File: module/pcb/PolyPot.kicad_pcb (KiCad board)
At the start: 2 copper layers, 50 x 50 mm, 43 parts, among them J1 V_BAT_1S, J2 PROG/DEBUG, J3 HUMIDITY_CONN, J4 TOF_DIST_SENS, J5 M3, J6 M3, J7 M3, J8 M3, J9 LUMINOSITY_CONN, M1 DC_WATER_PUMP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

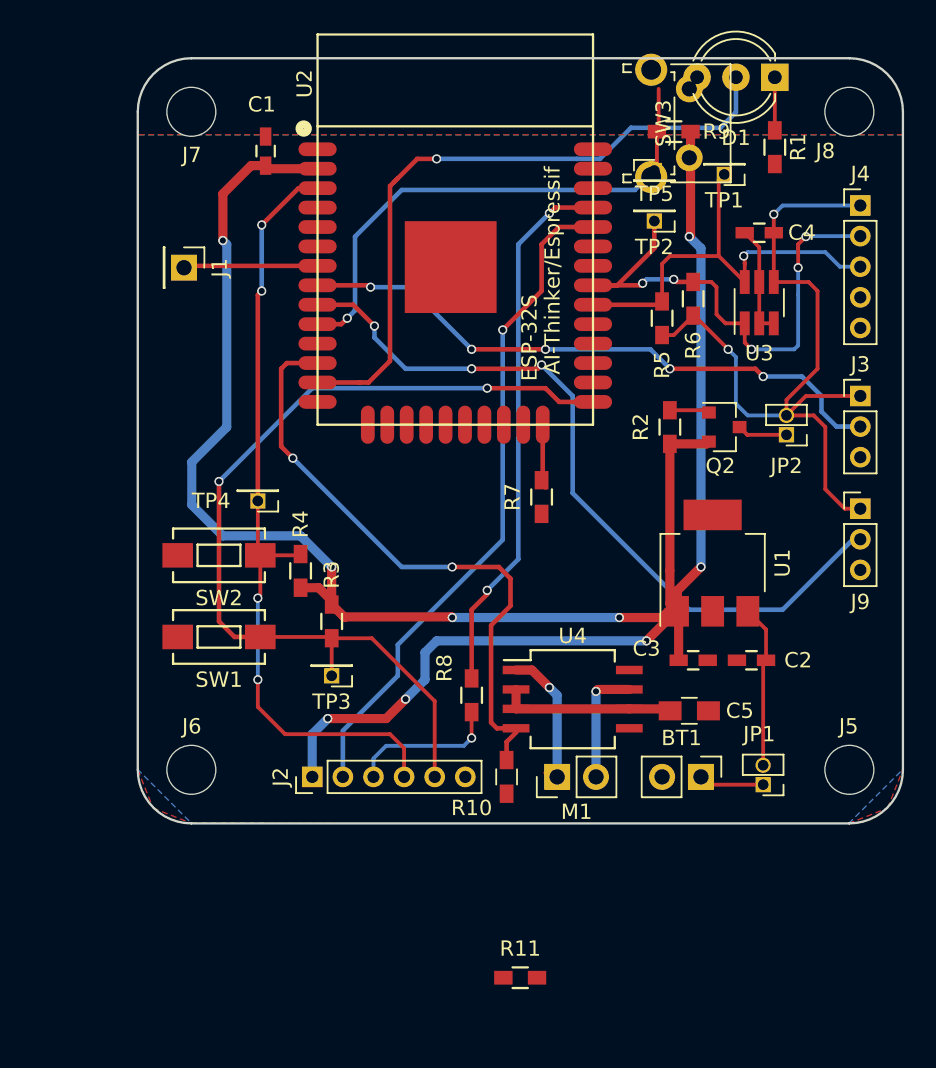
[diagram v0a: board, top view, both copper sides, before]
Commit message: PCB: change SOIC-8 footprint
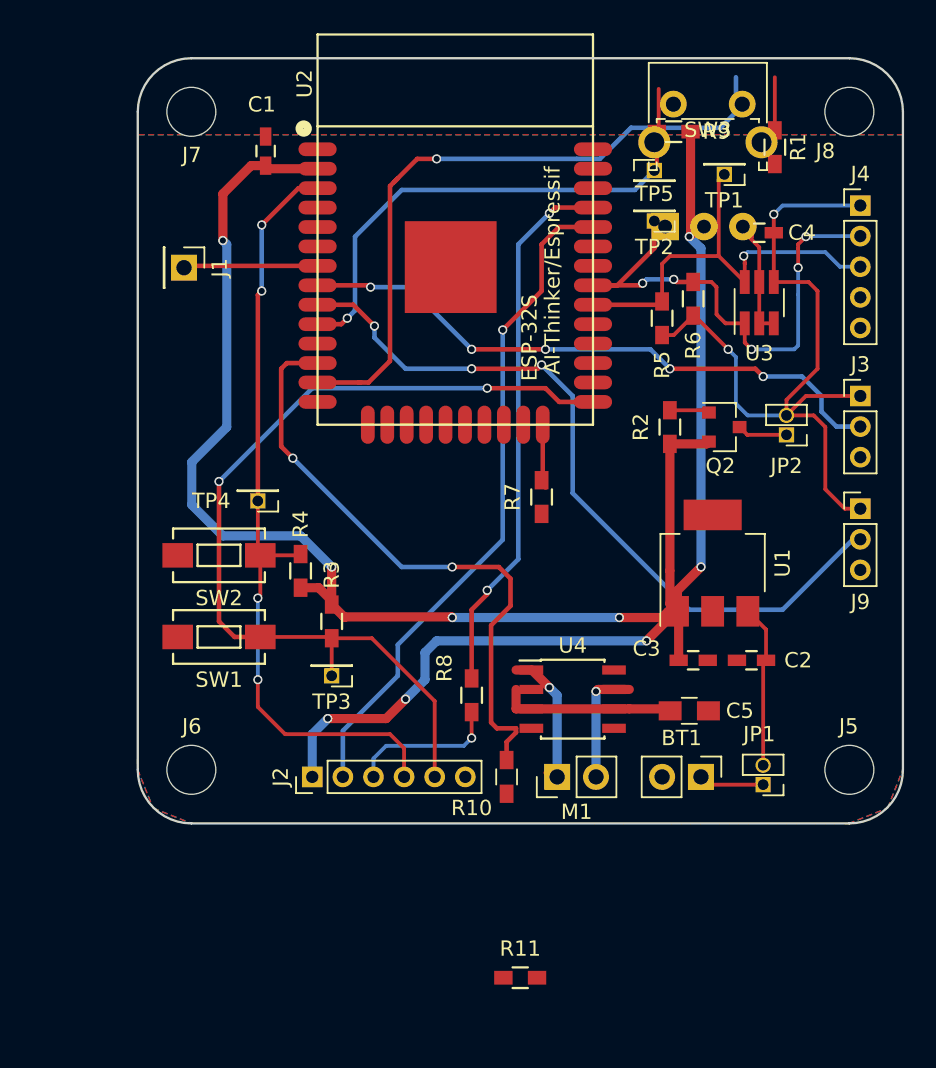
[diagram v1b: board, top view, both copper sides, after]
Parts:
- D1: moved to B.Cu
- U4: footprint Housings_SOIC:SO-8_5.3x6.2mm_Pitch1.27mm -> Housings_SOIC:SOIC-8_3.9x4.9mm_Pitch1.27mm
- moved D1 12.1 mm to (64.5, 41.0), turned to 0 degrees
- moved SW3 1.44 mm to (65.0, 33.0), turned to 0 degrees
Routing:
- net GND: track 51.6 -> 6.13 mm, vias 1 -> 0
- net /USER_BTN: track 34.4 -> 78.6 mm, vias 1 -> 2
- net Net-(D1-Pad3): track 0.00 -> 1.34 mm

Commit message: Add logo
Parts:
- removed TP1, TP2, TP3, TP4, TP5: TEST, Socket_Strips:Socket_Strip_Straight_1x01_Pitch1.27mm
- added G***: LOGO, PolyPot:PolyPot_13x20mm, B.Cu at (48.5, 57.5)
- added J10: I2C_TEST, Pin_Headers:Pin_Header_Straight_1x02_Pitch2.54mm, F.Cu at (55.0, 90.1)
- added REF***: OSHW-Logo2_9.8x8mm_SilkScreen, Symbols:OSHW-Logo2_9.8x8mm_SilkScreen, B.Cu at (62.5, 57.5)
- BT1, M1: footprint Socket_Strips:Socket_Strip_Straight_1x02_Pitch2.54mm -> Pin_Headers:Pin_Header_Straight_1x02_Pitch2.54mm
- J1: footprint Socket_Strips:Socket_Strip_Straight_1x01_Pitch2.54mm -> Pin_Headers:Pin_Header_Straight_1x01
- J2: footprint Socket_Strips:Socket_Strip_Straight_1x06_Pitch2.00mm -> Pin_Headers:Pin_Header_Straight_1x06_Pitch2.00mm
- J3, J9: footprint Socket_Strips:Socket_Strip_Straight_1x03_Pitch2.00mm -> Pin_Headers:Pin_Header_Straight_1x03_Pitch2.54mm
- J4: footprint Socket_Strips:Socket_Strip_Straight_1x05_Pitch2.00mm -> Pin_Headers:Pin_Header_Straight_1x05_Pitch2.54mm
- JP1, JP2: footprint Socket_Strips:Socket_Strip_Straight_1x02_Pitch1.27mm -> Pin_Headers:Pin_Header_Straight_1x02_Pitch2.54mm
- Q2: footprint TO_SOT_Packages_SMD:SOT-23 -> TO_SOT_Packages_SMD:SOT-23_Handsoldering
- moved J1 49.5 mm to (74.0, 71.5)
- moved J2 19.4 mm to (33.0, 59.5), turned to 0 degrees
- moved SW2 19.1 mm to (33.0, 43.5), turned to 90 degrees
- moved SW1 16.0 mm to (33.0, 52.0), turned to 90 degrees
- moved C1 14.2 mm to (24.5, 39.0)
- moved U4 13.9 mm to (44.5, 71.0)
- moved M1 13.9 mm to (43.5, 78.0), turned to 270 degrees
- moved J9 5.52 mm to (77.2, 65.0)
- moved J3 2.35 mm to (77.2, 54.4)
- moved U2 1.98 mm to (48.9, 45.8)
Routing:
- net (no net): track 0.16 -> 110.6 mm, vias 0 -> 6
- net /SENS_LUMINOSITY: track 50.0 -> 0.00 mm, vias 3 -> 0
- net /SENS_HUMIDITY: track 39.9 -> 0.00 mm, vias 5 -> 0
- net /USER_BTN: track 78.6 -> 44.1 mm, vias 2 -> 1
- net /3V3_SENSORS: track 50.7 -> 75.4 mm, vias 2 -> 7
- net GND: track 6.13 -> 21.1 mm
- net Net-(D1-Pad1): track 3.47 -> 15.9 mm, vias 0 -> 2
- net /I2C_SCL: track 35.1 -> 22.7 mm, vias 5 -> 3
- net +3V3: track 147.8 -> 138.0 mm, vias 9 -> 7
- net Net-(M1-Pad1): track 9.08 -> 0.00 mm, vias 1 -> 0
- net /V_BAT_SENSE: track 8.78 -> 0.00 mm
- net /PUMP_PWM: track 40.2 -> 48.3 mm, vias 2 -> 3
- net Net-(M1-Pad2): track 7.82 -> 0.00 mm, vias 1 -> 0
- net +BATT: track 15.7 -> 17.5 mm, vias 0 -> 1
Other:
- net class Default: via_drill 0.4 -> 0.3
- net class Power removed
- net class Signals removed

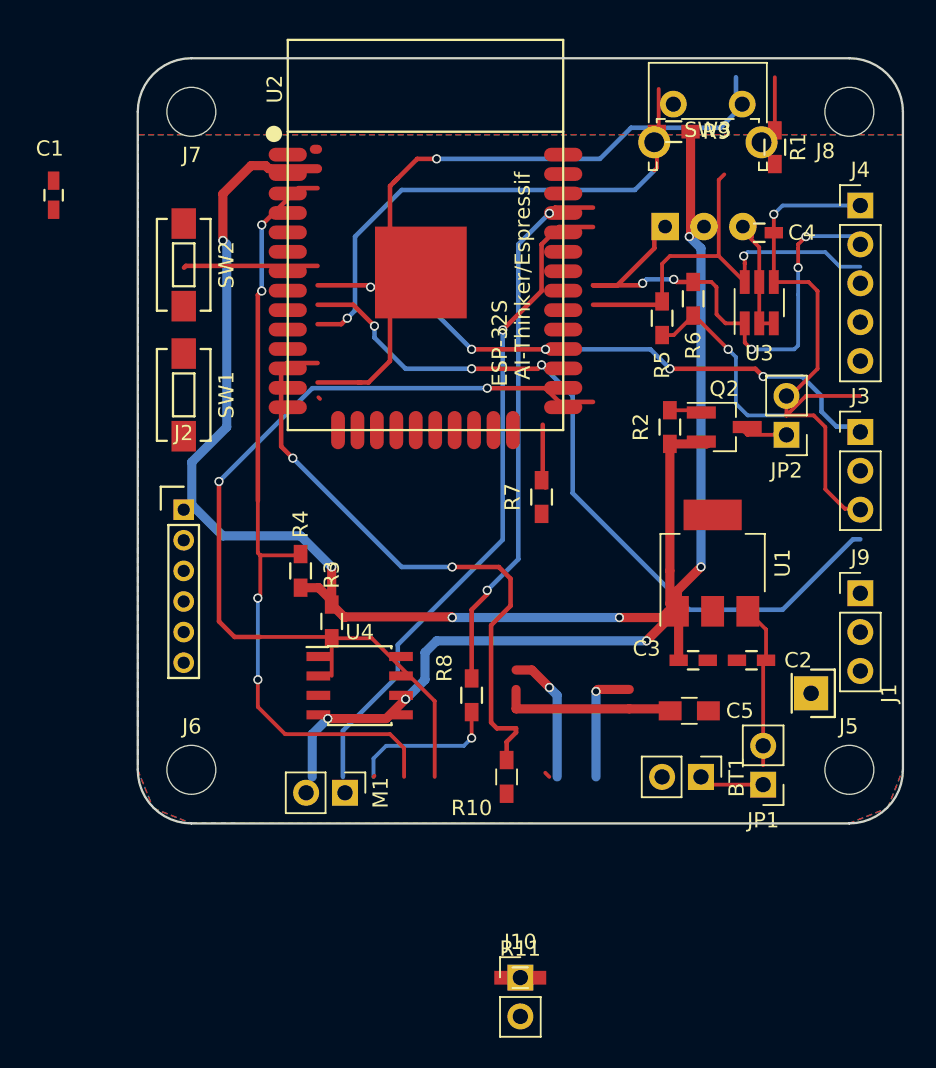
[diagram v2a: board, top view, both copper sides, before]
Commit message: PCB: fix 3.3V regulator footprint, connect TOF GPIO0, start routing
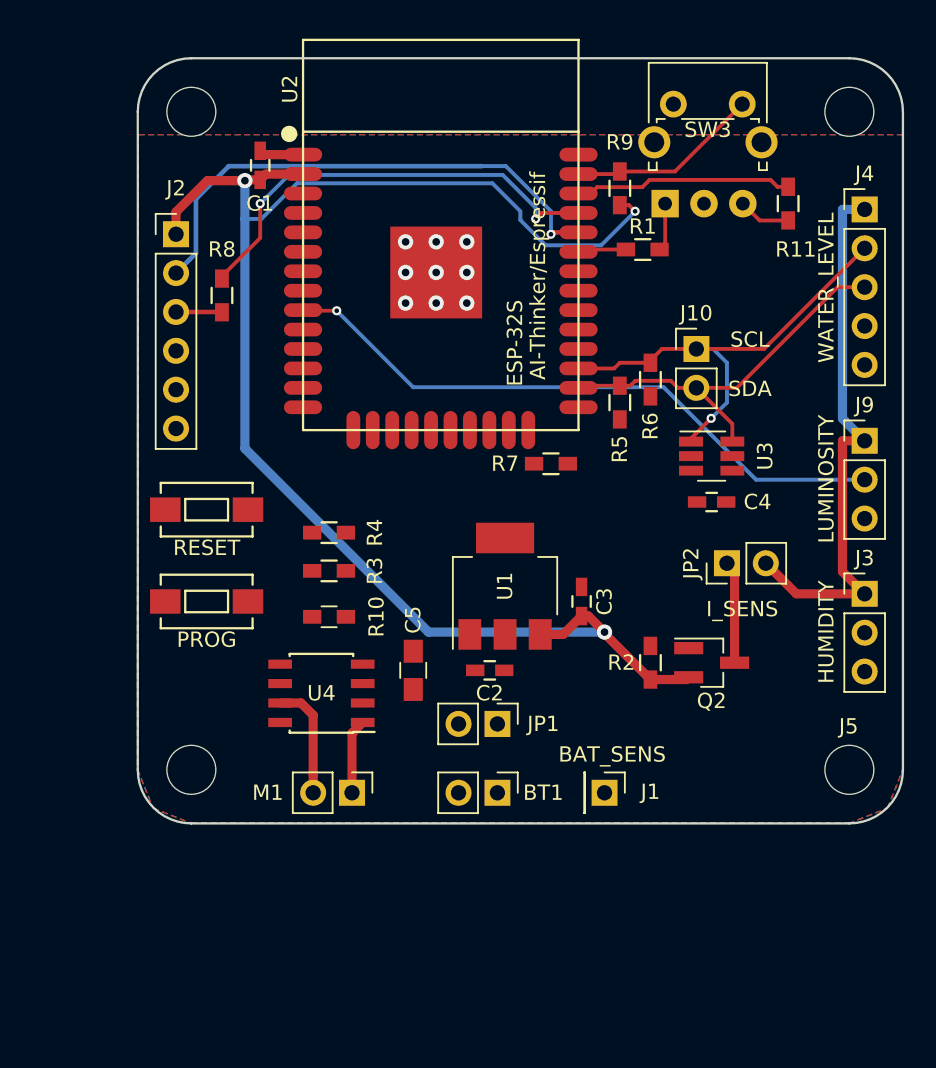
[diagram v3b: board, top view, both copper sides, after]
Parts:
- removed REF***: OSHW-Logo2_9.8x8mm_SilkScreen, Symbols:OSHW-Logo2_9.8x8mm_SilkScreen
- J1: footprint Pin_Headers:Pin_Header_Straight_1x01 -> Pin_Headers:Pin_Header_Straight_1x01_Pitch2.54mm
- J2: footprint Pin_Headers:Pin_Header_Straight_1x06_Pitch2.00mm -> Pin_Headers:Pin_Header_Straight_1x06_Pitch2.54mm
- U1: value AP7365-XXEG_SOT223 -> AP7365-XXERG_SOT223
- moved G*** 67.4 mm to (112.0, 35.0)
- moved R11 53.5 mm to (72.5, 39.5), turned to 90 degrees
- moved J10 42.7 mm to (66.5, 49.0)
- moved R8 30.8 mm to (35.5, 45.5)
- moved C5 18.2 mm to (48.0, 70.0), turned to 90 degrees
- moved J2 18.0 mm to (32.5, 41.5)
- moved C4 17.9 mm to (67.5, 59.0)
- moved JP1 17.8 mm to (53.5, 73.5), turned to 270 degrees
- moved C2 17.1 mm to (53.0, 70.0)
- moved SW2 16.1 mm to (34.5, 59.5), turned to 0 degrees
- moved R10 15.6 mm to (42.5, 66.5), turned to 180 degrees
- moved R2 15.5 mm to (63.5, 69.5)
- moved Q2 15.4 mm to (67.5, 69.5)
- moved J1 15.0 mm to (60.5, 78.0)
- moved U1 13.6 mm to (54.0, 64.5)
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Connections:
- BT1 pad 1: +BATT -> Net-(BT1-Pad1)
- C2 pad 1: Net-(C2-Pad1) -> +BATT
- J4 pad 4: (no net) -> /TOF_GPIO0
- JP1 pad 1: +BATT -> Net-(BT1-Pad1)
- JP1 pad 2: Net-(C2-Pad1) -> +BATT
- U1 pad 1: +3V3 -> GND
- U1 pad 2: GND -> +BATT
- U1 pad 3: Net-(C2-Pad1) -> +3V3
- U2 pad 10: /USER_BTN -> (no net)
- U2 pad 26: (no net) -> /I2C_SDA
- U2 pad 27: (no net) -> /I2C_SCL
- U2 pad 28: (no net) -> /TOF_GPIO0
- U2 pad 30: /I2C_SDA -> (no net)
- U2 pad 31: /I2C_SCL -> (no net)
- U2 pad 33: (no net) -> /LED_RED
- U2 pad 37: /LED_RED -> /USER_BTN
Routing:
- net (no net): track 110.6 -> 0.16 mm, vias 6 -> 0
- net /GPIO0: track 60.3 -> 0.00 mm, vias 2 -> 0
- net /EN: track 51.7 -> 0.00 mm, vias 4 -> 0
- net /PUMP_PWM: track 48.3 -> 0.00 mm, vias 3 -> 0
- net /SENS_LUMINOSITY: track 0.00 -> 41.3 mm, vias 0 -> 1
- net /3V3_SENSORS: track 75.4 -> 36.5 mm, vias 7 -> 0
- net +3V3: track 138.0 -> 99.3 mm, vias 7 -> 3
- net /USER_BTN: track 44.1 -> 12.6 mm, vias 1 -> 0
- net GND: track 21.1 -> 2.90 mm, vias 0 -> 9
- net +BATT: track 17.5 -> 0.00 mm, vias 1 -> 0
- net /LED_GREEN: track 0.00 -> 14.3 mm
- net Net-(D1-Pad1): track 15.9 -> 3.15 mm, vias 2 -> 0
- net Net-(C2-Pad1): track 10.6 -> 0.00 mm
- net /UART_RX: track 44.0 -> 34.0 mm
- net /I2C_SCL: track 22.7 -> 30.5 mm, vias 3 -> 1
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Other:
- board text added: "BAT_SENS"
- board text added: "HUMIDITY"
- board text added: "I_SENS"
- board text added: "LUMINOSITY"
- board text added: "SCL SDA"
- board text added: "WATER_LEVEL"

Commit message: PCB: routing almost done, silkscreen text
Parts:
- moved G*** 60.4 mm to (55.0, 55.0)
- moved R4 8.49 mm to (36.5, 55.0)
- moved R3 8.14 mm to (36.5, 58.0)
- moved R5 7.91 mm to (69.0, 50.0)
- moved R6 7.91 mm to (71.0, 48.5)
- moved SW1 2.00 mm to (34.5, 67.5)
- moved SW2 2.00 mm to (34.5, 61.5)
- moved R10 1.00 mm to (42.5, 67.5)
- moved U4 0.71 mm to (42.5, 72.0)
- moved J4 0.51 mm to (77.0, 40.0)
- moved J10 0.50 mm to (66.0, 49.0)
- moved J3 0.50 mm to (77.0, 65.0)
- moved J9 0.50 mm to (77.0, 55.0)
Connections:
- U2 pad 7: /V_BAT_SENSE -> /SENS_LUMINOSITY
- U2 pad 9: /SENS_LUMINOSITY -> /V_BAT_SENSE
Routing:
- net /V_BAT_SENSE: track 0.00 -> 66.1 mm, vias 0 -> 1
- net /GPIO0: track 0.00 -> 49.9 mm, vias 0 -> 1
- net /SENS_HUMIDITY: track 0.00 -> 47.5 mm, vias 0 -> 1
- net /EN: track 0.00 -> 30.5 mm
- net /PUMP_PWM: track 0.00 -> 23.6 mm
- net +BATT: track 0.00 -> 21.1 mm
- net /TOF_GPIO0: track 0.00 -> 18.8 mm, vias 0 -> 1
- net /3V3_SENSORS: track 36.5 -> 52.9 mm
- net GND: track 2.90 -> 16.1 mm
- net +3V3: track 99.3 -> 106.4 mm, vias 3 -> 4
- net Net-(BT1-Pad1): track 0.00 -> 4.50 mm
- net /SENSORS_ENn: track 0.00 -> 2.56 mm
- net Net-(R7-Pad2): track 0.00 -> 2.36 mm
- net /I2C_SCL: track 30.5 -> 29.8 mm
- net /I2C_SDA: track 26.3 -> 27.0 mm
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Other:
- board text added: "3.3V"
- board text added: "BAT+ -"
- board text added: "GND"
- board text added: "GPIO0"
- board text added: "HUM"
- board text added: "IO0"
- board text added: "I_SENSE"
- board text added: "LUM"
- board text added: "PROG"
- board text added: "PUMP"
- board text added: "RESET"
- board text added: "RXD"
- board text added: "SCL"
- board text added: "SDA"
- board text added: "TXD"
